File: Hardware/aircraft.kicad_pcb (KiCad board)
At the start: 4 copper layers, 100 x 50 mm, 190 parts, among them J1 Conn_01x02_Pin, J12 Conn_02x05_Odd_Even, J13 Conn_01x02, J14 USB_B_Micro, J15 Conn_02x05_Odd_Even, J16 USB_B_Micro, J17 USB_B_Micro, J18 USB_B_Micro, J19 U.FL-R-SMT-1_80_, J2 DM3AT-SF-PEJM5, J3 Conn_01x04, J4 Conn_01x04, J5 Conn_02x10_Odd_Even, J6 Conn_01x10, J7 Conn_01x04, J8 Conn_01x04, SW1 SW_SPDT, SW2 SW_Push_Dual, SW3 SW_SPDT, SW4 SW_Push_Dual, U1 MIC26903YJL-TR, U10 BMP390, U11 W25N01GVZEIG_TR, U12 STM32F405RGTx, U13 W25N01GVZEIG_TR, U14 24CW1280T-I/OT, U15 PCA9685PW_118, U16 CH330N, U17 CH330N, U2 LD39200PU33R, U3 INA226, U4 STM32F405RGTx, U5 IST8310, U6 NEO-M8N, U7 BMI088, U8 TMP100, U9 24CW1280T-I/OT, Y1 25MHz, Y2 25MHz

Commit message: sensors positioned
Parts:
- added JP5: SolderJumper_3_Open, Jumper:SolderJumper-3_P1.3mm_Open_RoundedPad1.0x1.5mm_NumberLabels, F.Cu at (204.6, 59.4)
- added JP6: SolderJumper_3_Open, Jumper:SolderJumper-3_P1.3mm_Open_RoundedPad1.0x1.5mm_NumberLabels, F.Cu at (197.3, 59.7)
- moved JP2 107.3 mm to (144.3, 87.6)
- moved C35 102.3 mm to (183.7, 67.2), turned to 180 degrees
- moved U7 96.4 mm to (176.5, 70.4)
- moved C34 96.3 mm to (178.0, 68.0), turned to 180 degrees
- moved U8 90.1 mm to (183.7, 69.4), turned to 180 degrees
- moved U10 85.3 mm to (153.1, 77.8)
- moved U5 83.3 mm to (151.5, 86.1)
- moved D1 77.0 mm to (152.5, 67.1)
- moved C29 75.0 mm to (153.8, 86.2), turned to 90 degrees
- moved C31 73.3 mm to (152.6, 83.8)
- moved C30 72.4 mm to (151.2, 88.4), turned to 180 degrees
- moved R3 70.2 mm to (154.5, 67.1)
- moved C37 69.9 mm to (155.0, 78.8), turned to 90 degrees
- moved C38 68.1 mm to (153.2, 75.9), turned to 180 degrees
- moved C32 60.1 mm to (142.2, 80.0), turned to -90 degrees
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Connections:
- J7 pad 1: +5V -> Net-(J7-Pin_1)
- J8 pad 1: +3.3V -> Net-(J8-Pin_1)
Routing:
- net GND: track 0.00 -> 76.4 mm, vias 0 -> 35
- net +3.3V: track 36.1 -> 61.7 mm, vias 25 -> 35
- net Net-(J13-Pin_1): track 0.00 -> 10.4 mm
- net Net-(U6-RF_IN): track 0.00 -> 8.90 mm
- net GPS_BACKUP_BAT: track 0.00 -> 8.56 mm
- net Net-(JP1-C): track 0.00 -> 5.38 mm
- net Net-(U6-VCC_RF): track 0.00 -> 3.35 mm
- net +5V: track 25.9 -> 28.3 mm, vias 60 -> 62
- net NU_GPS_NRST: track 0.00 -> 2.10 mm
- net Net-(L2-Pad2): track 0.00 -> 1.44 mm
- net Net-(U5-C1): track 0.00 -> 1.29 mm
- net Net-(D3-A): track 0.00 -> 1.02 mm
- net Net-(D1-A): track 0.00 -> 0.99 mm
- added copper zone on B.Cu, net GND

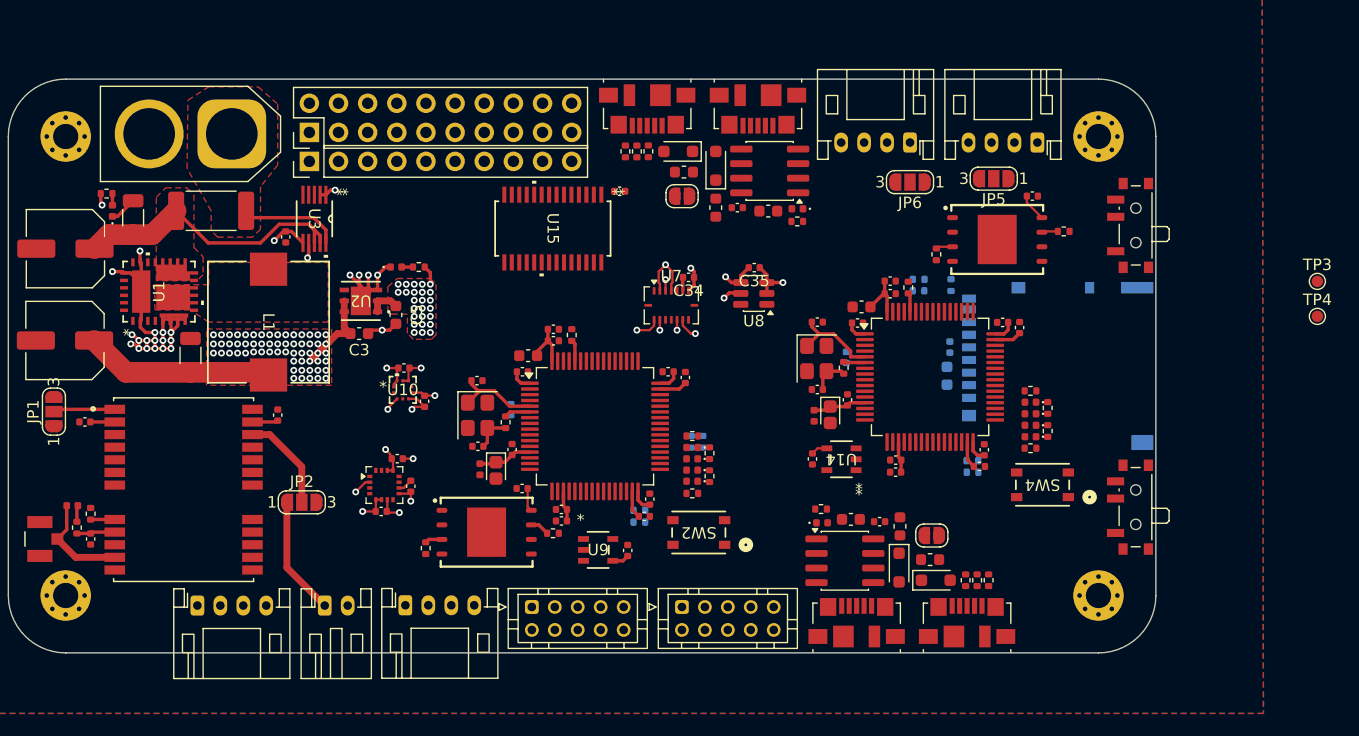
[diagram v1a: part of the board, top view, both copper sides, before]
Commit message: usb traces, i2c, spi, sdio, and more
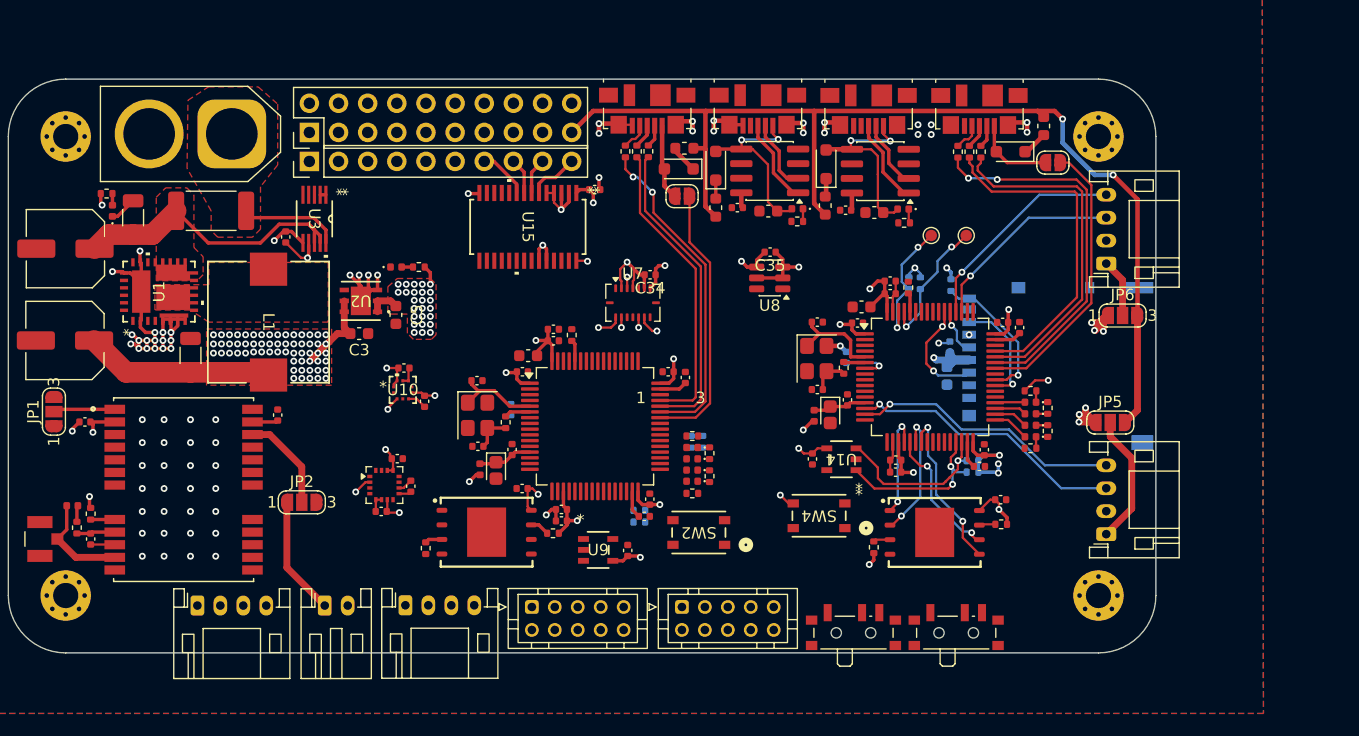
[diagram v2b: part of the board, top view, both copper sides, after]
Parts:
- moved J14 44.8 mm to (193.7, 53.3), turned to 180 degrees
- moved J16 44.8 mm to (203.3, 53.4), turned to 180 degrees
- moved FB4 39.1 mm to (208.9, 54.8), turned to 90 degrees
- moved SW3 38.4 mm to (201.3, 98.7), turned to 0 degrees
- moved D13 37.9 mm to (206.1, 57.0), turned to 180 degrees
- moved R48 37.4 mm to (201.5, 57.0), turned to -90 degrees
- moved R47 37.4 mm to (203.5, 57.0), turned to -90 degrees
- moved R46 37.4 mm to (202.5, 57.0), turned to -90 degrees
- moved D12 35.7 mm to (190.0, 58.1), turned to 90 degrees
- moved J8 34.6 mm to (214.4, 90.4), turned to 90 degrees
- moved JP3 34.2 mm to (209.8, 58.0), turned to 0 degrees
- moved U16 34.1 mm to (194.7, 58.7), turned to 180 degrees
- moved TP3 33.9 mm to (199.2, 64.3), turned to 90 degrees
- moved TP4 31.4 mm to (202.2, 64.3), turned to 90 degrees
- moved FB3 28.7 mm to (189.9, 61.7), turned to -90 degrees
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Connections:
- net NU_USB_OTG_FS_DM renamed NU_USB_OTG_FS_D-
- net NU_USB_OTG_FS_DP renamed NU_USB_OTG_FS_D+
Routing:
- net +5V: track 28.3 -> 123.4 mm, vias 62 -> 64
- net +3.3V: track 61.7 -> 113.5 mm, vias 35 -> 67
- net GND: track 76.4 -> 116.4 mm, vias 35 -> 81
- net FCU_USB_OTG_FS_ID: track 0.00 -> 32.8 mm, vias 0 -> 2
- net FCU_USB_OTG_FS_D-: track 0.00 -> 30.1 mm
- net FCU_USB_OTG_FS_D+: track 0.00 -> 29.4 mm
- net NU_USB_OTG_FS_ID: track 0.00 -> 28.7 mm, vias 0 -> 2
- net NU_USB_OTG_FS_D-: track 0.00 -> 27.0 mm
- net NU_USB_OTG_FS_D+: track 0.00 -> 26.3 mm
- net FCU_USB_OTG_FS_VBUS: track 0.00 -> 24.5 mm
- net FCU_UART4_TX: track 0.00 -> 24.2 mm, vias 0 -> 1
- net FCU_NRST: track 0.00 -> 24.2 mm, vias 0 -> 2
- net NU_USB_OTG_FS_VBUS: track 0.00 -> 23.7 mm
- net FCU_UART4_RX: track 0.00 -> 23.6 mm, vias 0 -> 1
- net FCU_UART3_RX: track 0.00 -> 19.0 mm, vias 0 -> 1
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
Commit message: i2c sensors traces
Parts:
- moved C27 32.5 mm to (109.8, 61.9)
- moved C8 32.5 mm to (108.4, 56.9)
- moved R7 32.5 mm to (107.5, 54.9)
- moved C4 32.5 mm to (111.3, 61.7)
- moved C9 32.5 mm to (103.3, 59.9)
- moved D2 32.5 mm to (106.0, 65.1)
- moved R1 32.5 mm to (109.8, 64.2)
- moved R4 32.5 mm to (108.5, 62.2)
- moved R5 32.5 mm to (108.2, 58.5)
- moved R6 32.5 mm to (103.6, 55.9)
- moved C6 32.5 mm to (105.3, 61.1)
- moved R36 16.5 mm to (105.6, 82.7)
- moved R37 16.5 mm to (105.6, 84.6)
- moved R39 16.5 mm to (105.6, 88.6)
- moved R40 16.5 mm to (105.6, 90.6)
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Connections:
- U4 pad 10: NU_SPI2_MISO -> unconnected-(U4-PC2-Pad10)
- U4 pad 11: NU_SPI2_MOSI -> unconnected-(U4-PC3-Pad11)
- U4 pad 33: NU_SPI2_CS_IMU -> unconnected-(U4-PB12-Pad33)
- U4 pad 34: NU_SPI2_SCK -> unconnected-(U4-PB13-Pad34)
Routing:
- net NU_I2C2_SCL: track 0.00 -> 73.8 mm, vias 0 -> 6
- net NU_I2C2_SDA: track 0.00 -> 66.2 mm, vias 0 -> 5
- net NU_MAG_INT: track 0.00 -> 17.9 mm, vias 0 -> 2
- net NU_SPI1_MISO: track 0.00 -> 15.8 mm, vias 0 -> 2
- net NU_BARO_INT: track 0.00 -> 14.1 mm, vias 0 -> 2
- net NU_SPI1_FLASH_CS: track 0.00 -> 14.0 mm, vias 0 -> 2
- net NU_SPI1_SCK: track 0.00 -> 11.1 mm, vias 0 -> 2
- net NU_SPI1_MOSI: track 0.00 -> 11.0 mm, vias 0 -> 2
- net GND: track 116.4 -> 124.2 mm, vias 81 -> 82
- net NU_I2C3_SCL: track 0.00 -> 7.02 mm, vias 0 -> 1
- net NU_I2C3_SDA: track 0.00 -> 5.60 mm, vias 0 -> 1
- net NU_NRST: track 0.00 -> 4.59 mm, vias 0 -> 1
- net FCU_NRST: track 24.2 -> 20.5 mm
- net NU_LED_4: track 0.00 -> 3.47 mm
- net NU_LED_3: track 0.00 -> 3.20 mm
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
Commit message: idk what i did here
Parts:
- moved C29 0.12 mm to (153.9, 86.2)
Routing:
- net FCU_SWDIO: track 0.00 -> 64.3 mm, vias 0 -> 2
- net FCU_SWCLK: track 0.00 -> 59.7 mm, vias 0 -> 2
- net NU_I2C3_SCL: track 7.02 -> 48.7 mm
- net NU_UART2_RX: track 0.00 -> 40.7 mm, vias 0 -> 2
- net NU_I2C3_SDA: track 5.60 -> 44.9 mm
- net NU_UART2_TX: track 0.00 -> 38.5 mm, vias 0 -> 2
- net NU_SWDIO: track 0.00 -> 32.2 mm, vias 0 -> 2
- net NU_SWCLK: track 0.00 -> 30.4 mm, vias 0 -> 2
- net FCU_UART2_RX: track 0.00 -> 27.9 mm, vias 0 -> 2
- net FCU_UART2_TX: track 0.00 -> 26.1 mm, vias 0 -> 2
- net GND: track 124.2 -> 145.7 mm, vias 82 -> 97
- net NU_NRST: track 4.59 -> 23.2 mm, vias 1 -> 2
- net NU_UART4_TX: track 0.00 -> 18.5 mm, vias 0 -> 1
- net NU_UART4_RX: track 0.00 -> 17.8 mm, vias 0 -> 1
- net FCU_NRST: track 20.5 -> 37.0 mm
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
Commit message: starting layout again...
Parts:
- removed the REF** at (213.7, 95.7)
- removed the REF** at (123.7, 95.7)
- removed the REF** at (213.7, 55.7)
- removed the REF** at (123.7, 55.7)
- added REF**: MountingHole_3.2mm_M3_Pad_Via, MountingHole:MountingHole_3.2mm_M3_Pad_Via, F.Cu at (155.0, 90.0)
- added REF**: MountingHole_3.2mm_M3_Pad_Via, MountingHole:MountingHole_3.2mm_M3_Pad_Via, F.Cu at (155.0, 45.0)
- added REF**: MountingHole_3.2mm_M3_Pad_Via, MountingHole:MountingHole_3.2mm_M3_Pad_Via, F.Cu at (249.2, 45.0)
- added REF**: MountingHole_3.2mm_M3_Pad_Via, MountingHole:MountingHole_3.2mm_M3_Pad_Via, F.Cu at (249.1, 90.0)
- C27, C4, C53, C57, C58, C6, C8, D2, R1, R29, R30, R31, R32, R4, R5, R54: moved to F.Cu
- R11: moved to B.Cu
- moved JP5 182.5 mm to (34.2, 54.4)
- moved JP6 182.1 mm to (34.2, 57.9)
- moved FB4 164.1 mm to (47.7, 85.3), turned to 0 degrees
- moved D14 161.1 mm to (38.9, 94.3), turned to 0 degrees
- moved U13 160.0 mm to (43.8, 53.5)
- moved C55 159.0 mm to (50.5, 50.7)
- moved D13 157.5 mm to (52.2, 90.6), turned to 0 degrees
- moved R33 156.8 mm to (53.4, 50.7), turned to 0 degrees
- moved JP3 155.7 mm to (56.9, 88.0)
- moved U16 154.7 mm to (41.4, 79.9), turned to 0 degrees
- moved C60 153.3 mm to (41.8, 94.3), turned to 0 degrees
- moved D17 152.5 mm to (38.9, 96.3), turned to 0 degrees
- moved C58 151.6 mm to (50.5, 54.6), turned to 0 degrees
- moved R54 148.2 mm to (53.4, 54.6), turned to 0 degrees
- moved C61 147.3 mm to (47.7, 77.8), turned to 0 degrees
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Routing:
- net +5V: track 123.4 -> 0.00 mm, vias 64 -> 0
- net GND: track 145.7 -> 30.6 mm, vias 97 -> 8
- net +3.3V: track 123.6 -> 51.9 mm, vias 73 -> 18
- net FCU_SWDIO: track 64.3 -> 0.00 mm, vias 2 -> 0
- net FCU_SWCLK: track 59.7 -> 0.00 mm, vias 2 -> 0
- net NU_I2C3_SCL: track 48.7 -> 4.22 mm
- net NU_UART2_RX: track 40.7 -> 0.00 mm, vias 2 -> 0
- net NU_I2C3_SDA: track 44.9 -> 4.17 mm
- net NU_UART2_TX: track 38.5 -> 0.00 mm, vias 2 -> 0
- net FCU_NRST: track 37.0 -> 0.00 mm, vias 2 -> 0
- net FCU_USB_OTG_FS_ID: track 32.8 -> 0.00 mm, vias 2 -> 0
- net NU_SWDIO: track 32.2 -> 0.00 mm, vias 2 -> 0
- net NU_SWCLK: track 30.4 -> 0.00 mm, vias 2 -> 0
- net FCU_USB_OTG_FS_D-: track 30.1 -> 0.00 mm
- net FCU_USB_OTG_FS_D+: track 29.4 -> 0.00 mm
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- removed copper zone on F.Cu, net +3.3V
- removed copper zone on F.Cu, net +5V
- removed copper zone on In2.Cu, net +5V
- removed copper zone on F.Cu, net PS_CS
- removed copper zone on F.Cu, net PS_PVIN
- removed copper zone on F.Cu, net VIN+
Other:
- board size 100 x 50 mm -> 104.2 x 55 mm
- board text added: "10,42cmx5,5cm"
